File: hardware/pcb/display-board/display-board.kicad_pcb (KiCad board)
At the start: 4 copper layers, 92 x 30 mm, 51 parts, among them J1 Conn_01x01_Socket, J2 Conn_01x01_Socket, J3 Conn_01x01_Socket, J4 Conn_01x01_Socket, J5 Conn_01x01_Socket, J6 Conn_01x01_Socket, Q1 AO3400A, Q2 AO3401A, Q3 AO3400A, Q4 AO3401A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

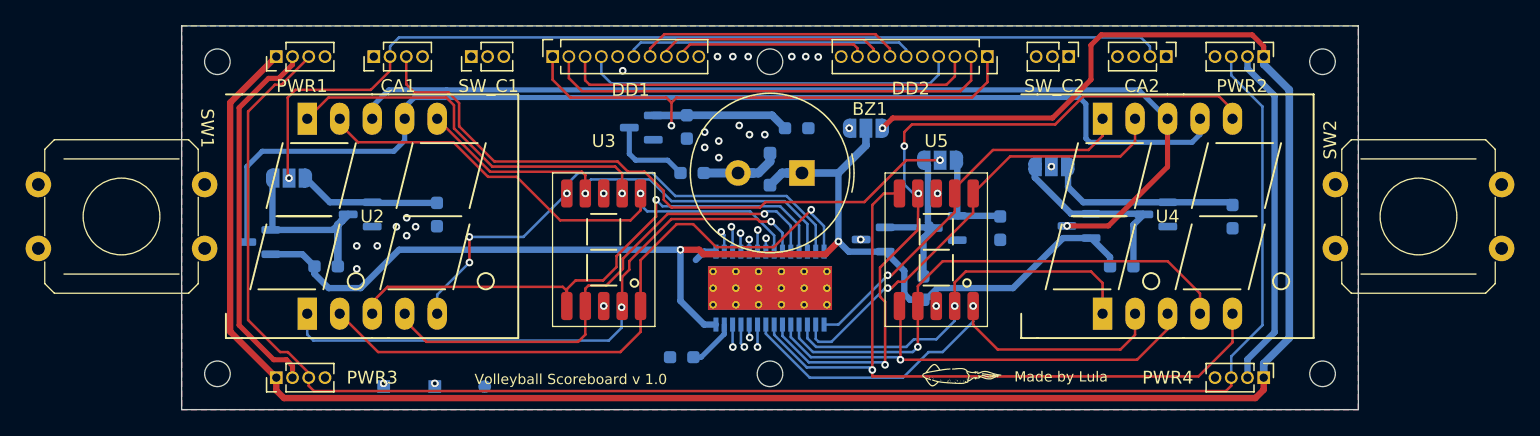
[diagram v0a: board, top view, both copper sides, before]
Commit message: Added main board to the hw folder, some 3d models for the inner structure and the code itself
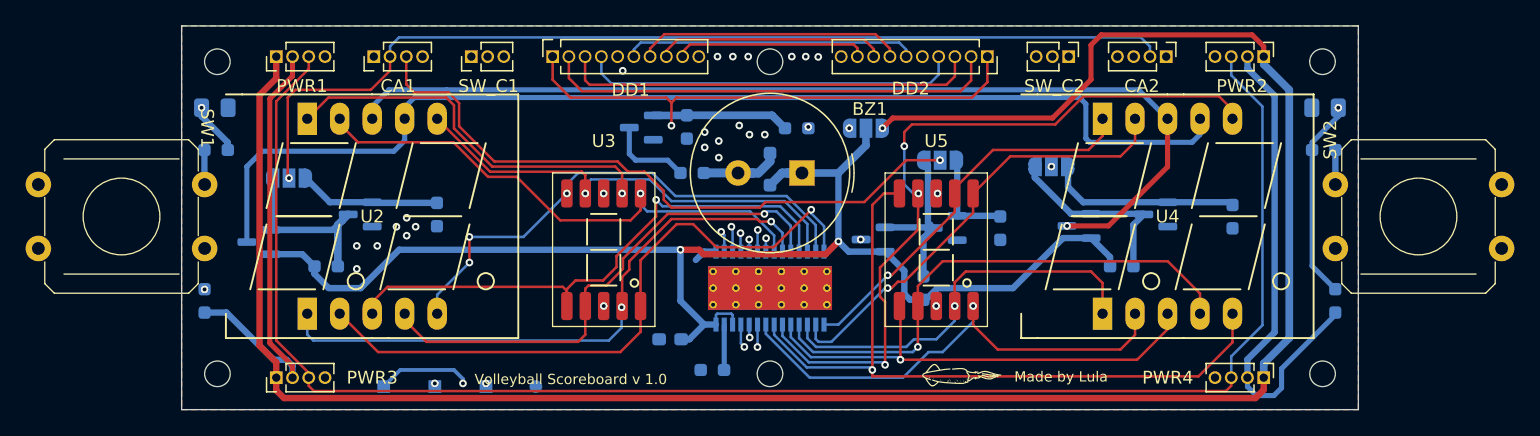
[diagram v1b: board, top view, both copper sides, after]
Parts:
- added C1: C, Capacitor_SMD:C_0603_1608Metric_Pad1.08x0.95mm_HandSolder, B.Cu at (92.2, 107.0)
- added C2: 0.1uF, Capacitor_SMD:C_0805_2012Metric_Pad1.18x1.45mm_HandSolder, B.Cu at (143.4, 88.9)
- added C3: 0.1uF, Capacitor_SMD:C_0805_2012Metric_Pad1.18x1.45mm_HandSolder, B.Cu at (56.6, 88.9)
- added CTRL: TestPoint_Pad_1.0x1.0mm, TestPoint:TestPoint_Pad_1.0x1.0mm, B.Cu at (69.8, 110.7)
- added R11: 1k, Resistor_SMD:R_0603_1608Metric_Pad0.98x0.95mm_HandSolder, B.Cu at (143.3, 92.2)
- added R12: 100k, Resistor_SMD:R_0603_1608Metric_Pad0.98x0.95mm_HandSolder, B.Cu at (144.2, 104.0)
- added R13: 1k, Resistor_SMD:R_0603_1608Metric_Pad0.98x0.95mm_HandSolder, B.Cu at (56.7, 92.2)
- added R14: 100k, Resistor_SMD:R_0603_1608Metric_Pad0.98x0.95mm_HandSolder, B.Cu at (55.8, 104.0)
- moved BAT+ 4.00 mm to (77.8, 110.7)
- moved GND 4.00 mm to (81.7, 110.7)
- moved LDO 4.00 mm to (73.8, 110.7)
- moved R4 2.60 mm to (95.5, 109.4)
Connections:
- DD1 pad 2: /DCPRG -> /CTRL
- DD2 pad 2: /DCPRG -> /CTRL
- PWR1 pad 3: /CTRL -> /BUZZER
- PWR2 pad 3: /CTRL -> /BUZZER
- PWR3 pad 3: /CTRL -> /BUZZER
- PWR4 pad 3: /CTRL -> /BUZZER
- SW1 pad 1: /SW1 -> Net-(R13-Pad1)
- SW2 pad 2: /SW2 -> Net-(R11-Pad1)
- U1 pad 26: /DCPRG -> VCC
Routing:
- net /BUZZER: track 0.00 -> 164.1 mm, vias 0 -> 1
- net /DCPRG: track 67.5 -> 0.00 mm, vias 1 -> 0
- net /CTRL: track 130.5 -> 72.6 mm, vias 0 -> 1
- net /LDO: track 176.7 -> 198.6 mm
- net /SW1: track 79.0 -> 94.8 mm, vias 0 -> 2
- net /SW2: track 79.5 -> 90.6 mm, vias 0 -> 1
- net VCC: track 98.8 -> 103.9 mm
- net Net-(R13-Pad1): track 0.00 -> 2.71 mm
- net Net-(R11-Pad1): track 0.00 -> 2.70 mm
- net /BAT+: track 184.8 -> 186.5 mm
- net /XLAT: track 47.9 -> 48.6 mm
